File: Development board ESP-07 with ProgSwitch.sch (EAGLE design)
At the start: 10 parts, among them Q1 BSS138, Q2 BSS138, SW1 KSS-2EG4430

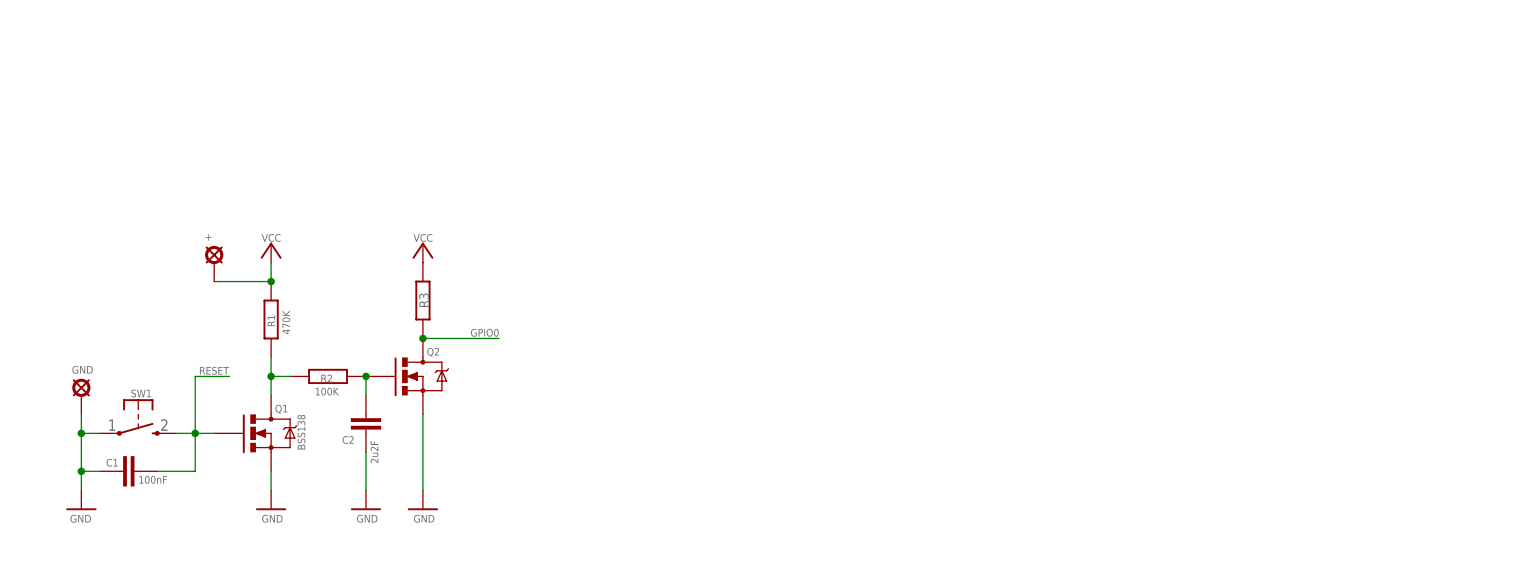
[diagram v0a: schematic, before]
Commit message: Minor cosmetic changes
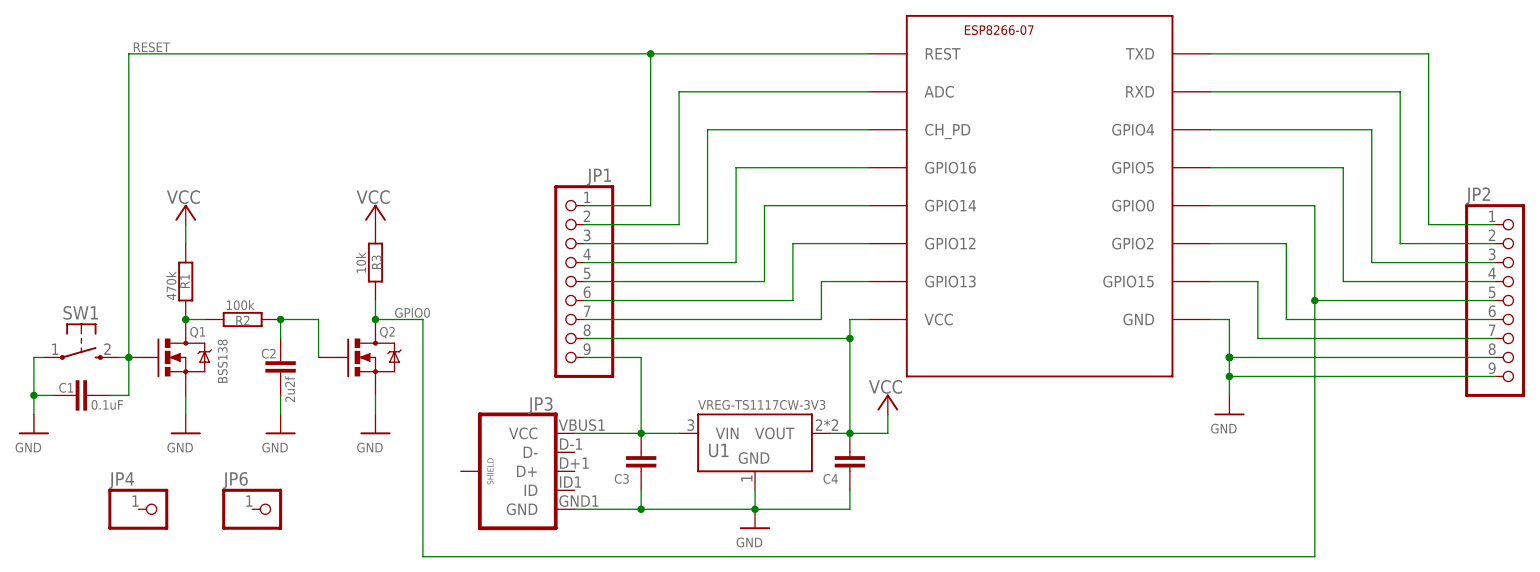
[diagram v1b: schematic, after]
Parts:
- removed +, GND: LSP10, solpad:LSP10
- added C3, C4: (no value), rcl:C-EU025-024X044
- added ESP8266-07: ESP8266-07, lio:ESP8266-07
- added JP1, JP2: (no value), pinhead+:PINHD-1X91X09_SMT
- added JP3: (no value), SparkFun-Connectors:USB_MICROB_PLUGCONN-11752
- added JP4, JP6: (no value), pinhead+:PINHD-1X1
- added U1: VREG-TS1117CW-3V3, we-power:VREG-TS1117CW-3V3
- C1: value 100nF -> 0.1uF
- C2: value 2u2F -> 2u2f
- R1: value 470K -> 470k; device rcl:R-EU_R0805 -> rcl:R-EU_R1206
- R2: value 100K -> 100k; device rcl:R-EU_R0805 -> rcl:R-EU_R1206
- R3: value (none) -> 10k; device rcl:R-EU_R0805 -> rcl:R-EU_R1206
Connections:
- new net N$1: ESP8266-07.TXD, JP2.1
- new net N$11: ESP8266-07.ADC, JP1.2
- new net N$12: ESP8266-07.CH_PD, JP1.3
- new net N$13: ESP8266-07.GPIO16, JP1.4
- new net N$14: ESP8266-07.GPIO14, JP1.5
- new net N$15: ESP8266-07.GPIO12, JP1.6
- new net N$16: C3.2, JP1.9, JP3.VCC, U1.VIN
- new net N$17: ESP8266-07.GPIO13, JP1.7
- new net N$2: ESP8266-07.RXD, JP2.2
- new net N$24: ESP8266-07.GPIO4, JP2.3
- new net N$5: ESP8266-07.GPIO5, JP2.4
- new net N$6: ESP8266-07.VCC, JP1.8
- new net N$7: ESP8266-07.GPIO2, JP2.6
- new net N$8: ESP8266-07.GPIO15, JP2.7
- net GND: now also C3.1, C4.1, ESP8266-07.GND, JP2.8, JP2.9, JP3.GND, U1.GND; no longer GND.MP
- net GPIO0: now also ESP8266-07.GPIO0, JP2.5
- net RESET: now also ESP8266-07.REST, JP1.1
- net VCC: now also C4.2, U1.VOUT; no longer +.MP
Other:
- moved on the sheet: C1, C2, Q1, Q2, R1, R2, R3, SW1
